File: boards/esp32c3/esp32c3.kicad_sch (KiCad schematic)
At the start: 26 parts, among them J1 USB-C, J2 IO, Q1 AO3401A, SW1 RESET, SW2 BOOT, U1 ESP32-C3-WROOM-02-N4, U2 LP38693MP-3.3

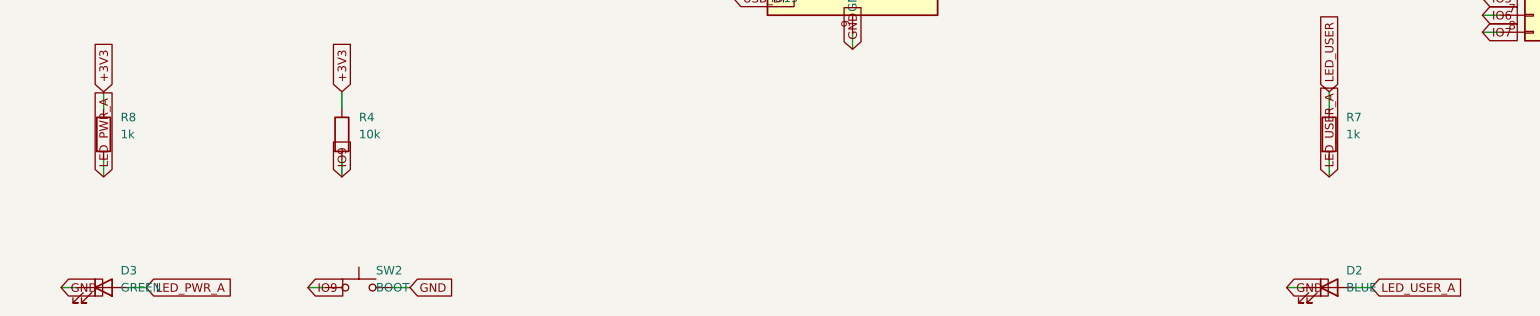
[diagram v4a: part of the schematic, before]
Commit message: review: datasheet design review on the netlist; fixes a reversed TVS and dim LEDs
lib/review.py checks the design intent that ERC and the netlist check take
on trust: diode/TVS polarity against inferred rail voltages, LED current
from the JLC Vf range, per-datasheet decoupling and supply ranges, USB-C
CC pull-downs and D+/D- on both sides, ESP32-C3 EN RC, strapping pins and
GPIO18/19, relay flyback path and pickup voltage, capacitor rating and
polarity. It runs after the netlist check and stops the build on ERROR.
lib/review_test.py breaks the real netlists 15 ways; every rule fires and
the unmodified boards report no ERROR.

Real defects it found:
- usbc-ldo: SMAJ5.0A had anode on +5V and cathode on GND (KiCad names
  the cathode pin "A1"), shorting the rail on plug-in. Swapped.
- esp32c3: blue user LED on a 3.3 V GPIO (Vf 2.5-3.6 V) -> yellow, 470R.
- esp32c3, relay8: green power LED at ~0.45 mA through 1k -> 220R.
- usbc-ldo: SS32 symbol for an SS34 part -> Diode:SS34.

Also: lcsc-check.json keeps JLC attributes (Vf, voltage rating) for the
review; lcsc.py groups parts from net.txt instead of fab/groups.json; the
build retries freerouting (up to 3 runs) because it is not deterministic
and occasionally leaves two connections unrouted on the same DSN.
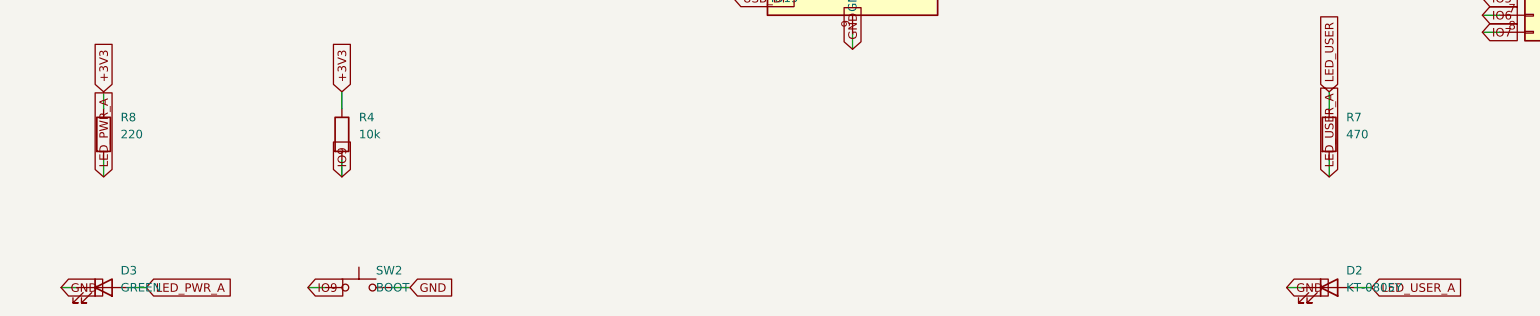
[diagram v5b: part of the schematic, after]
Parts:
- D2: value BLUE -> KT-0805Y
- R7: value 1k -> 470
- R8: value 1k -> 220
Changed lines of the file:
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@@
 		(instances
 			(project ""
-				(path "/96b8dbc3-e12b-4040-ab5e-4ba71b553fe6"
+				(path "/6b105ba3-351c-4bc0-85ea-73316523c341"
 					(reference "J1")
 					(unit 1)
@@
 		(instances
 			(project ""
-				(path "/96b8dbc3-e12b-4040-ab5e-4ba71b553fe6"
+				(path "/6b105ba3-351c-4bc0-85ea-73316523c341"
 					(reference "R1")
 					(unit 1)
@@
 		(instances
 			(project ""
-				(path "/96b8dbc3-e12b-4040-ab5e-4ba71b553fe6"
+				(path "/6b105ba3-351c-4bc0-85ea-73316523c341"
 					(reference "R2")
 					(unit 1)
@@
 		(instances
 			(project ""
-				(path "/96b8dbc3-e12b-4040-ab5e-4ba71b553fe6"
+				(path "/6b105ba3-351c-4bc0-85ea-73316523c341"
 					(reference "D1")
 					(unit 1)
@@
 		(instances
 			(project ""
-				(path "/96b8dbc3-e12b-4040-ab5e-4ba71b553fe6"
+				(path "/6b105ba3-351c-4bc0-85ea-73316523c341"
 					(reference "#FLG04")
 					(unit 1)
@@
 		(instances
 			(project ""
-				(path "/96b8dbc3-e12b-4040-ab5e-4ba71b553fe6"
+				(path "/6b105ba3-351c-4bc0-85ea-73316523c341"
 					(reference "#FLG05")
 					(unit 1)
@@
 		(instances
 			(project ""
-				(path "/96b8dbc3-e12b-4040-ab5e-4ba71b553fe6"
+				(path "/6b105ba3-351c-4bc0-85ea-73316523c341"
 					(reference "U2")
 					(unit 1)
@@
 		(instances
 			(project ""
-				(path "/96b8dbc3-e12b-4040-ab5e-4ba71b553fe6"
+				(path "/6b105ba3-351c-4bc0-85ea-73316523c341"
 					(reference "C1")
 					(unit 1)
@@
 		(instances
 			(project ""
-				(path "/96b8dbc3-e12b-4040-ab5e-4ba71b553fe6"
+				(path "/6b105ba3-351c-4bc0-85ea-73316523c341"
 					(reference "C2")
 					(unit 1)
@@
 		(instances
 			(project ""
-				(path "/96b8dbc3-e12b-4040-ab5e-4ba71b553fe6"
+				(path "/6b105ba3-351c-4bc0-85ea-73316523c341"
 					(reference "C3")
 					(unit 1)
@@
 		(instances
 			(project ""
-				(path "/96b8dbc3-e12b-4040-ab5e-4ba71b553fe6"
+				(path "/6b105ba3-351c-4bc0-85ea-73316523c341"
 					(reference "Q1")
 					(unit 1)
@@
 		(instances
 			(project ""
-				(path "/96b8dbc3-e12b-4040-ab5e-4ba71b553fe6"
+				(path "/6b105ba3-351c-4bc0-85ea-73316523c341"
 					(reference "R9")
 					(unit 1)
@@
 		(instances
 			(project ""
-				(path "/96b8dbc3-e12b-4040-ab5e-4ba71b553fe6"
+				(path "/6b105ba3-351c-4bc0-85ea-73316523c341"
 					(reference "C6")
 					(unit 1)
@@
 		(instances
 			(project ""
-				(path "/96b8dbc3-e12b-4040-ab5e-4ba71b553fe6"
+				(path "/6b105ba3-351c-4bc0-85ea-73316523c341"
 					(reference "C7")
 					(unit 1)
@@
 		(instances
 			(project ""
-				(path "/96b8dbc3-e12b-4040-ab5e-4ba71b553fe6"
+				(path "/6b105ba3-351c-4bc0-85ea-73316523c341"
 					(reference "C5")
 					(unit 1)
@@
 		(instances
 			(project ""
-				(path "/96b8dbc3-e12b-4040-ab5e-4ba71b553fe6"
+				(path "/6b105ba3-351c-4bc0-85ea-73316523c341"
 					(reference "#FLG15")
 					(unit 1)
@@
 		(instances
 			(project ""
-				(path "/96b8dbc3-e12b-4040-ab5e-4ba71b553fe6"
+				(path "/6b105ba3-351c-4bc0-85ea-73316523c341"
 					(reference "U1")
 					(unit 1)
@@
 		(instances
 			(project ""
-				(path "/96b8dbc3-e12b-4040-ab5e-4ba71b553fe6"
+				(path "/6b105ba3-351c-4bc0-85ea-73316523c341"
 					(reference "R3")
 					(unit 1)
@@
 		(instances
 			(project ""
-				(path "/96b8dbc3-e12b-4040-ab5e-4ba71b553fe6"
+				(path "/6b105ba3-351c-4bc0-85ea-73316523c341"
 					(reference "C4")
 					(unit 1)
@@
 		(instances
 			(project ""
-				(path "/96b8dbc3-e12b-4040-ab5e-4ba71b553fe6"
+				(path "/6b105ba3-351c-4bc0-85ea-73316523c341"
 					(reference "SW1")
 					(unit 1)
@@
 		(instances
 			(project ""
-				(path "/96b8dbc3-e12b-4040-ab5e-4ba71b553fe6"
+				(path "/6b105ba3-351c-4bc0-85ea-73316523c341"
 					(reference "R4")
 					(unit 1)
@@
 		(instances
 			(project ""
-				(path "/96b8dbc3-e12b-4040-ab5e-4ba71b553fe6"
+				(path "/6b105ba3-351c-4bc0-85ea-73316523c341"
 					(reference "SW2")
 					(unit 1)
@@
 		(instances
 			(project ""
-				(path "/96b8dbc3-e12b-4040-ab5e-4ba71b553fe6"
+				(path "/6b105ba3-351c-4bc0-85ea-73316523c341"
 					(reference "R5")
 					(unit 1)
@@
 		(instances
 			(project ""
-				(path "/96b8dbc3-e12b-4040-ab5e-4ba71b553fe6"
+				(path "/6b105ba3-351c-4bc0-85ea-73316523c341"
 					(reference "R6")
 					(unit 1)
@@
 			(effects (font (size 1.27 1.27)) (justify left))
 		)
-		(property "Value" "1k"
+		(property "Value" "470"
 			(at 289.56 139.7 0)
 			(effects (font (size 1.27 1.27)) (justify left))
@@
 		(instances
 			(project ""
-				(path "/96b8dbc3-e12b-4040-ab5e-4ba71b553fe6"
+				(path "/6b105ba3-351c-4bc0-85ea-73316523c341"
 					(reference "R7")
 					(unit 1)
@@
 			(effects (font (size 1.27 1.27)) (justify left))
 		)
-		(property "Value" "BLUE"
+		(property "Value" "KT-0805Y"
 			(at 289.56 162.56 0)
 			(effects (font (size 1.27 1.27)) (justify left))
@@
 		(instances
 			(project ""
-				(path "/96b8dbc3-e12b-4040-ab5e-4ba71b553fe6"
+				(path "/6b105ba3-351c-4bc0-85ea-73316523c341"
 					(reference "D2")
 					(unit 1)
@@
 			(effects (font (size 1.27 1.27)) (justify left))
 		)
-		(property "Value" "1k"
+		(property "Value" "220"
 			(at 106.68 139.7 0)
 			(effects (font (size 1.27 1.27)) (justify left))
@@
 		(instances
 			(project ""
-				(path "/96b8dbc3-e12b-4040-ab5e-4ba71b553fe6"
+				(path "/6b105ba3-351c-4bc0-85ea-73316523c341"
 					(reference "R8")
 					(unit 1)
@@
 		(instances
 			(project ""
-				(path "/96b8dbc3-e12b-4040-ab5e-4ba71b553fe6"
+				(path "/6b105ba3-351c-4bc0-85ea-73316523c341"
 					(reference "D3")
 					(unit 1)
@@
 		(instances
 			(project ""
-				(path "/96b8dbc3-e12b-4040-ab5e-4ba71b553fe6"
+				(path "/6b105ba3-351c-4bc0-85ea-73316523c341"
 					(reference "J2")
 					(unit 1)
